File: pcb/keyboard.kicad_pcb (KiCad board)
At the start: 2 copper layers, 6 parts

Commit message: Modified layout further
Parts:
- removed H1, H2, H3, H4, H5, H6: MountingHole, MountingHole:MountingHole_3.2mm_M3
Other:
- board outline added: 242.5 x 98.2 mm

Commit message: Working on schematic and PCB
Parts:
- added C1: 1u, Capacitor_SMD:C_0402_1005Metric, F.Cu at (153.3, 238.3)
- added C10: 4.7u, Capacitor_SMD:C_0603_1608Metric, F.Cu at (149.8, 200.7)
- added C11: 100nF, Capacitor_SMD:C_0603_1608Metric, F.Cu at (149.8, 203.2)
- added C2: 100nF, Capacitor_SMD:C_0603_1608Metric, F.Cu at (153.9, 236.1)
- added C3: 1u, Capacitor_SMD:C_0402_1005Metric, F.Cu at (153.3, 240.3)
- added C4: 33p, Capacitor_SMD:C_0805_2012Metric, F.Cu at (160.7, 205.4)
- added C5: 33p, Capacitor_SMD:C_0805_2012Metric, F.Cu at (160.7, 208.4)
- added C6: 10n, Capacitor_SMD:C_0603_1608Metric, F.Cu at (149.8, 190.7)
- added C7: 100nF, Capacitor_SMD:C_0603_1608Metric, F.Cu at (149.8, 193.2)
- added C8: 100nF, Capacitor_SMD:C_0603_1608Metric, F.Cu at (149.8, 195.7)
- added C9: 1u, Capacitor_SMD:C_0603_1608Metric, F.Cu at (149.8, 198.2)
- added D1: D_Small, Diode_SMD:D_SOD-123, F.Cu at (35.7, 270.1)
- added D10: D_Small, Diode_SMD:D_SOD-123, F.Cu at (41.5, 270.1)
- added D11: D_Small, Diode_SMD:D_SOD-123, F.Cu at (41.5, 273.4)
- added D12: D_Small, Diode_SMD:D_SOD-123, F.Cu at (41.5, 276.8)
- added D13: D_Small, Diode_SMD:D_SOD-123, F.Cu at (41.5, 280.1)
- added D14: D_Small, Diode_SMD:D_SOD-123, F.Cu at (41.5, 283.5)
- added D15: D_Small, Diode_SMD:D_SOD-123, F.Cu at (41.5, 286.9)
- added D16: D_Small, Diode_SMD:D_SOD-123, F.Cu at (41.5, 290.2)
- added D17: D_Small, Diode_SMD:D_SOD-123, F.Cu at (41.5, 293.6)
- added D18: D_Small, Diode_SMD:D_SOD-123, F.Cu at (41.5, 296.9)
- added D19: D_Small, Diode_SMD:D_SOD-123, F.Cu at (47.3, 270.1)
- added D2: D_Small, Diode_SMD:D_SOD-123, F.Cu at (35.7, 273.4)
- added D20: D_Small, Diode_SMD:D_SOD-123, F.Cu at (47.3, 273.4)
- added D21: D_Small, Diode_SMD:D_SOD-123, F.Cu at (47.3, 276.8)
- added D22: D_Small, Diode_SMD:D_SOD-123, F.Cu at (47.3, 280.1)
- added D23: D_Small, Diode_SMD:D_SOD-123, F.Cu at (47.3, 283.5)
- added D24: D_Small, Diode_SMD:D_SOD-123, F.Cu at (47.3, 286.9)
- added D25: D_Small, Diode_SMD:D_SOD-123, F.Cu at (47.3, 290.2)
- added D26: D_Small, Diode_SMD:D_SOD-123, F.Cu at (47.3, 293.6)
- added D27: D_Small, Diode_SMD:D_SOD-123, F.Cu at (47.3, 296.9)
- added D28: D_Small, Diode_SMD:D_SOD-123, F.Cu at (53.1, 270.1)
- added D29: D_Small, Diode_SMD:D_SOD-123, F.Cu at (53.1, 273.4)
- added D3: D_Small, Diode_SMD:D_SOD-123, F.Cu at (35.7, 276.8)
- added D30: D_Small, Diode_SMD:D_SOD-123, F.Cu at (53.1, 276.8)
- added D31: D_Small, Diode_SMD:D_SOD-123, F.Cu at (53.1, 280.1)
- added D32: D_Small, Diode_SMD:D_SOD-123, F.Cu at (53.1, 283.5)
- added D33: D_Small, Diode_SMD:D_SOD-123, F.Cu at (53.1, 286.9)
- added D34: D_Small, Diode_SMD:D_SOD-123, F.Cu at (53.1, 290.2)
- added D35: D_Small, Diode_SMD:D_SOD-123, F.Cu at (53.1, 293.6)
- added D36: D_Small, Diode_SMD:D_SOD-123, F.Cu at (53.1, 296.9)
- added D37: D_Small, Diode_SMD:D_SOD-123, F.Cu at (58.9, 270.1)
- added D38: D_Small, Diode_SMD:D_SOD-123, F.Cu at (58.9, 273.4)
- added D39: D_Small, Diode_SMD:D_SOD-123, F.Cu at (58.9, 276.8)
- added D4: D_Small, Diode_SMD:D_SOD-123, F.Cu at (35.7, 280.1)
- added D40: D_Small, Diode_SMD:D_SOD-123, F.Cu at (58.9, 280.1)
- added D41: D_Small, Diode_SMD:D_SOD-123, F.Cu at (58.9, 283.5)
- added D42: D_Small, Diode_SMD:D_SOD-123, F.Cu at (58.9, 286.9)
- added D5: D_Small, Diode_SMD:D_SOD-123, F.Cu at (35.7, 283.5)
- added D6: D_Small, Diode_SMD:D_SOD-123, F.Cu at (35.7, 286.9)
- added D7: D_Small, Diode_SMD:D_SOD-123, F.Cu at (35.7, 290.2)
- added D8: D_Small, Diode_SMD:D_SOD-123, F.Cu at (35.7, 293.6)
- added D9: D_Small, Diode_SMD:D_SOD-123, F.Cu at (35.7, 296.9)
- added H1: MountingHole, MountingHole:MountingHole_3.2mm_M3, F.Cu at (105.0, 55.3)
- added H2: MountingHole, MountingHole:MountingHole_3.2mm_M3, F.Cu at (116.4, 113.7)
- added H3: MountingHole, MountingHole:MountingHole_3.2mm_M3, F.Cu at (200.0, 76.3)
- added H4: MountingHole, MountingHole:MountingHole_3.2mm_M3, F.Cu at (200.0, 136.1)
- added H5: MountingHole, MountingHole:MountingHole_3.2mm_M3, F.Cu at (295.0, 55.3)
- added H6: MountingHole, MountingHole:MountingHole_3.2mm_M3, F.Cu at (283.6, 113.7)
- added J1: USB_C_Receptacle_USB2.0, local-library:TYPE-C-31-M-12, F.Cu at (157.8, 218.2)
- added J2: Conn_01x04, Connector_PinHeader_2.54mm:PinHeader_1x04_P2.54mm_Vertical, F.Cu at (150.2, 214.2)
- added L1: 10u, Inductor_SMD:L_0805_2012Metric, F.Cu at (165.2, 205.2)
- added R1: 10.2k, Resistor_SMD:R_0201_0603Metric, F.Cu at (153.7, 222.2)
- added R2: 10.2k, Resistor_SMD:R_0201_0603Metric, F.Cu at (153.7, 224.0)
- added R3: 10.2k, Resistor_SMD:R_0201_0603Metric, F.Cu at (153.7, 225.7)
- added R4: 10.2k, Resistor_SMD:R_0201_0603Metric, F.Cu at (153.7, 227.5)
- added SW1: SW_Push, local-library:SW_PG1350, F.Cu at (96.3, 64.1)
- added SW10: SW_Push, local-library:SW_PG1350, F.Cu at (148.4, 68.1)
- added SW11: SW_Push, local-library:SW_PG1350, F.Cu at (144.8, 84.9)
- added SW12: SW_Push, local-library:SW_PG1350, F.Cu at (141.2, 101.8)
- added SW13: SW_Push, local-library:SW_PG1350, F.Cu at (137.6, 118.7)
- added SW14: SW_Push, local-library:SW_PG1350, F.Cu at (164.7, 74.1)
- added SW15: SW_Push, local-library:SW_PG1350, F.Cu at (161.1, 91.0)
- added SW16: SW_Push, local-library:SW_PG1350, F.Cu at (157.5, 107.8)
- added SW17: SW_Push, local-library:SW_PG1350, F.Cu at (154.0, 124.7)
- added SW18: SW_Push, local-library:SW_PG1350, F.Cu at (182.0, 75.7)
- added SW19: SW_Push, local-library:SW_PG1350, F.Cu at (178.4, 92.6)
- added SW2: SW_Push, local-library:SW_PG1350, F.Cu at (92.7, 81.0)
- added SW20: SW_Push, local-library:SW_PG1350, F.Cu at (174.8, 109.5)
- added SW21: SW_Push, local-library:SW_PG1350, F.Cu at (177.9, 133.6)
- added SW22: SW_Push, local-library:SW_PG1350, F.Cu at (218.0, 75.7)
- added SW23: SW_Push, local-library:SW_PG1350, F.Cu at (221.6, 92.6)
- added SW24: SW_Push, local-library:SW_PG1350, F.Cu at (225.2, 109.5)
- added SW25: SW_Push, local-library:SW_PG1350, F.Cu at (222.1, 133.6)
- added SW26: SW_Push, local-library:SW_PG1350, F.Cu at (235.3, 74.1)
- added SW27: SW_Push, local-library:SW_PG1350, F.Cu at (238.9, 91.0)
- added SW28: SW_Push, local-library:SW_PG1350, F.Cu at (242.5, 107.8)
- added SW29: SW_Push, local-library:SW_PG1350, F.Cu at (246.0, 124.7)
- added SW3: SW_Push, local-library:SW_PG1350, F.Cu at (89.1, 97.9)
- added SW30: SW_Push, local-library:SW_PG1350, F.Cu at (251.6, 68.1)
- added SW31: SW_Push, local-library:SW_PG1350, F.Cu at (255.2, 84.9)
- added SW32: SW_Push, local-library:SW_PG1350, F.Cu at (258.8, 101.8)
- added SW33: SW_Push, local-library:SW_PG1350, F.Cu at (262.4, 118.7)
- added SW34: SW_Push, local-library:SW_PG1350, F.Cu at (269.0, 66.9)
- added SW35: SW_Push, local-library:SW_PG1350, F.Cu at (272.6, 83.8)
- added SW36: SW_Push, local-library:SW_PG1350, F.Cu at (276.2, 100.7)
- added SW37: SW_Push, local-library:SW_PG1350, F.Cu at (286.4, 65.8)
- added SW38: SW_Push, local-library:SW_PG1350, F.Cu at (290.0, 82.6)
- added SW39: SW_Push, local-library:SW_PG1350, F.Cu at (293.6, 99.5)
- added SW4: SW_Push, local-library:SW_PG1350, F.Cu at (113.6, 65.8)
- added SW40: SW_Push, local-library:SW_PG1350, F.Cu at (303.7, 64.1)
- added SW41: SW_Push, local-library:SW_PG1350, F.Cu at (307.3, 81.0)
- added SW42: SW_Push, local-library:SW_PG1350, F.Cu at (310.9, 97.9)
- added SW5: SW_Push, local-library:SW_PG1350, F.Cu at (110.0, 82.6)
- added SW6: SW_Push, local-library:SW_PG1350, F.Cu at (106.4, 99.5)
- added SW7: SW_Push, local-library:SW_PG1350, F.Cu at (131.0, 66.9)
- added SW8: SW_Push, local-library:SW_PG1350, F.Cu at (127.4, 83.8)
- added SW9: SW_Push, local-library:SW_PG1350, F.Cu at (123.8, 100.7)
- added TP1: TestPoint, TestPoint:TestPoint_Pad_D2.0mm, F.Cu at (149.8, 232.4)
- added TP2: TestPoint, TestPoint:TestPoint_Pad_D2.0mm, F.Cu at (149.8, 236.4)
- added TP3: TestPoint, TestPoint:TestPoint_Pad_D2.0mm, F.Cu at (149.8, 240.5)
- added U1: LP3993-33B3F, Package_TO_SOT_SMD:SOT-23, F.Cu at (154.3, 232.6)
- added U2: USBLC6-2SC6, Package_TO_SOT_SMD:SOT-23-6, F.Cu at (157.5, 223.6)
- added U3: STM32F411RETx, Package_QFP:LQFP-64_10x10mm_P0.5mm, F.Cu at (159.1, 196.7)
- added Y1: 12MHz, Crystal:Crystal_SMD_5032-4Pin_5.0x3.2mm, F.Cu at (155.2, 206.3)

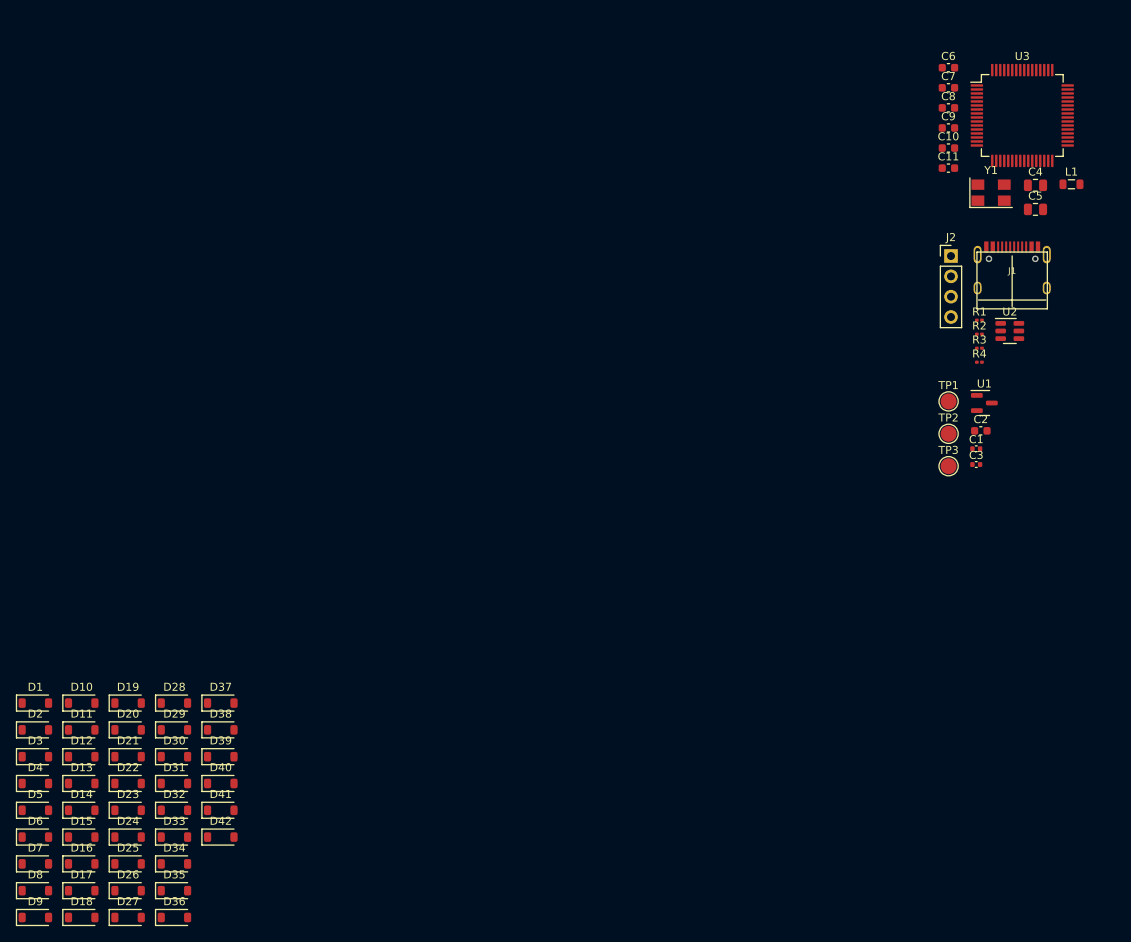
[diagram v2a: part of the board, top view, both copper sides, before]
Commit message: Finished off schematic
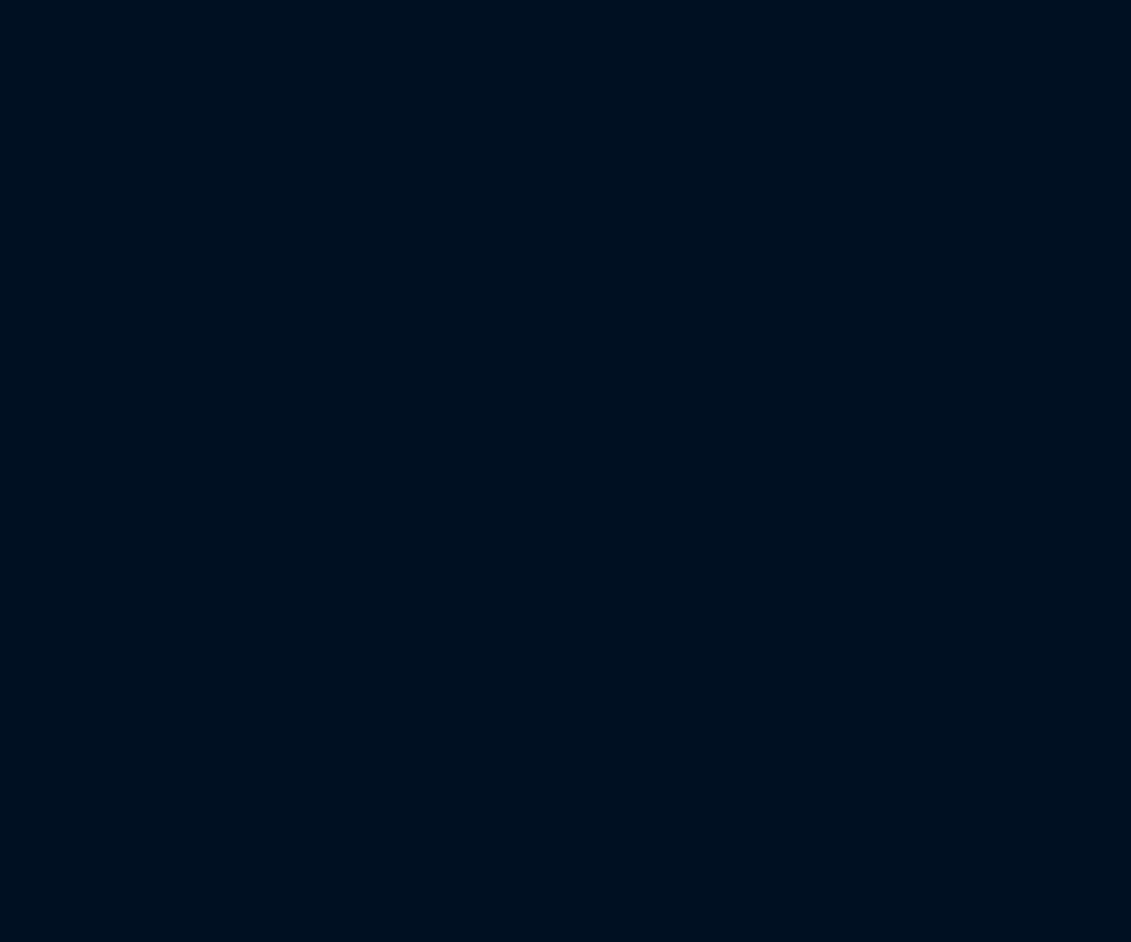
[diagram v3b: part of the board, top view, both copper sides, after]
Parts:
- removed C1, C3: 1u, Capacitor_SMD:C_0402_1005Metric
- removed C10: 4.7u, Capacitor_SMD:C_0603_1608Metric
- removed C11, C2, C7, C8: 100nF, Capacitor_SMD:C_0603_1608Metric
- removed C4, C5: 33p, Capacitor_SMD:C_0805_2012Metric
- removed C6: 10n, Capacitor_SMD:C_0603_1608Metric
- removed C9: 1u, Capacitor_SMD:C_0603_1608Metric
- removed D1, D10, D11, D12, D13, D14, D15, D16, D17, D18, D19, D2, D20, D21, D22, D23, D24, D25, D26, D27, D28, D29, D3, D30, D31, D32, D33, D34, D35, D36, D37, D38, D39, D4, D40, D41, D42, D5, D6, D7, D8, D9: D_Small, Diode_SMD:D_SOD-123
- removed J1: USB_C_Receptacle_USB2.0, local-library:TYPE-C-31-M-12
- removed J2: Conn_01x04, Connector_PinHeader_2.54mm:PinHeader_1x04_P2.54mm_Vertical
- removed L1: 10u, Inductor_SMD:L_0805_2012Metric
- removed R1, R2, R3, R4: 10.2k, Resistor_SMD:R_0201_0603Metric
- removed TP1, TP2, TP3: TestPoint, TestPoint:TestPoint_Pad_D2.0mm
- removed U1: LP3993-33B3F, Package_TO_SOT_SMD:SOT-23
- removed U2: USBLC6-2SC6, Package_TO_SOT_SMD:SOT-23-6
- removed U3: STM32F411RETx, Package_QFP:LQFP-64_10x10mm_P0.5mm
- removed Y1: 12MHz, Crystal:Crystal_SMD_5032-4Pin_5.0x3.2mm

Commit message: Started routing
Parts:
- added C1: 10n, Capacitor_SMD:C_0603_1608Metric, F.Cu at (192.5, 83.3)
- added C10: 10n, Capacitor_SMD:C_0603_1608Metric, F.Cu at (191.1, 97.6)
- added C11: 100nF, Capacitor_SMD:C_0603_1608Metric, F.Cu at (191.1, 102.4)
- added C12: 100nF, Capacitor_SMD:C_0603_1608Metric, F.Cu at (203.9, 107.7)
- added C13: 1u, Capacitor_SMD:C_0603_1608Metric, F.Cu at (211.8, 97.2)
- added C14: 4.7u, Capacitor_SMD:C_0603_1608Metric, F.Cu at (208.3, 102.8)
- added C15: 100nF, Capacitor_SMD:C_0603_1608Metric, B.Cu at (199.7, 102.0)
- added C16: 1u, Capacitor_SMD:C_0603_1608Metric, F.Cu at (197.5, 89.0)
- added C2: 100n, Capacitor_SMD:C_0603_1608Metric, F.Cu at (196.5, 83.3)
- added C3: 10u, Capacitor_SMD:C_0805_2012Metric, F.Cu at (194.5, 86.2)
- added C4: 1u, Capacitor_SMD:C_0603_1608Metric, F.Cu at (191.5, 86.8)
- added C5: 100nF, Capacitor_SMD:C_0603_1608Metric, F.Cu at (191.5, 90.2)
- added C6: 33p, Capacitor_SMD:C_0805_2012Metric, F.Cu at (195.8, 111.8)
- added C7: 15p, Capacitor_SMD:C_0805_2012Metric, F.Cu at (196.5, 115.8)
- added C8: 33p, Capacitor_SMD:C_0805_2012Metric, F.Cu at (204.2, 111.8)
- added C9: 15p, Capacitor_SMD:C_0805_2012Metric, F.Cu at (203.5, 115.8)
- added D1: D_Small, Diode_SMD:D_SOD-123, B.Cu at (101.4, 70.5)
- added D10: D_Small, Diode_SMD:D_SOD-123, B.Cu at (153.5, 74.4)
- added D11: D_Small, Diode_SMD:D_SOD-123, B.Cu at (149.9, 91.3)
- added D12: D_Small, Diode_SMD:D_SOD-123, B.Cu at (146.3, 108.2)
- added D13: D_Small, Diode_SMD:D_SOD-123, B.Cu at (142.7, 125.0)
- added D14: D_Small, Diode_SMD:D_SOD-123, B.Cu at (169.9, 80.4)
- added D15: D_Small, Diode_SMD:D_SOD-123, B.Cu at (166.3, 97.3)
- added D16: D_Small, Diode_SMD:D_SOD-123, B.Cu at (162.7, 114.2)
- added D17: D_Small, Diode_SMD:D_SOD-123, B.Cu at (159.1, 131.1)
- added D18: D_Small, Diode_SMD:D_SOD-123, B.Cu at (187.1, 82.1)
- added D19: D_Small, Diode_SMD:D_SOD-123, B.Cu at (183.6, 98.9)
- added D2: D_Small, Diode_SMD:D_SOD-123, B.Cu at (97.8, 87.4)
- added D20: D_Small, Diode_SMD:D_SOD-123, B.Cu at (180.0, 115.8)
- added D21: D_Small, Diode_SMD:D_SOD-123, B.Cu at (181.2, 141.1)
- added D22: D_Small, Diode_SMD:D_SOD-123, B.Cu at (225.3, 79.4)
- added D23: D_Small, Diode_SMD:D_SOD-123, B.Cu at (228.9, 96.3)
- added D24: D_Small, Diode_SMD:D_SOD-123, B.Cu at (232.5, 113.2)
- added D25: D_Small, Diode_SMD:D_SOD-123, B.Cu at (230.1, 135.3)
- added D26: D_Small, Diode_SMD:D_SOD-123, B.Cu at (242.6, 77.8)
- added D27: D_Small, Diode_SMD:D_SOD-123, B.Cu at (246.2, 94.7)
- added D28: D_Small, Diode_SMD:D_SOD-123, B.Cu at (249.7, 111.5)
- added D29: D_Small, Diode_SMD:D_SOD-123, B.Cu at (253.3, 128.4)
- added D3: D_Small, Diode_SMD:D_SOD-123, B.Cu at (94.3, 104.2)
- added D30: D_Small, Diode_SMD:D_SOD-123, B.Cu at (258.9, 71.8)
- added D31: D_Small, Diode_SMD:D_SOD-123, B.Cu at (262.5, 88.6)
- added D32: D_Small, Diode_SMD:D_SOD-123, B.Cu at (266.1, 105.5)
- added D33: D_Small, Diode_SMD:D_SOD-123, B.Cu at (269.7, 122.4)
- added D34: D_Small, Diode_SMD:D_SOD-123, B.Cu at (276.3, 70.6)
- added D35: D_Small, Diode_SMD:D_SOD-123, B.Cu at (279.9, 87.5)
- added D36: D_Small, Diode_SMD:D_SOD-123, B.Cu at (283.5, 104.4)
- added D37: D_Small, Diode_SMD:D_SOD-123, B.Cu at (293.7, 69.5)
- added D38: D_Small, Diode_SMD:D_SOD-123, B.Cu at (297.3, 86.4)
- added D39: D_Small, Diode_SMD:D_SOD-123, B.Cu at (300.9, 103.2)
- added D4: D_Small, Diode_SMD:D_SOD-123, B.Cu at (118.7, 72.1)
- added D40: D_Small, Diode_SMD:D_SOD-123, B.Cu at (311.0, 67.9)
- added D41: D_Small, Diode_SMD:D_SOD-123, B.Cu at (314.6, 84.7)
- added D42: D_Small, Diode_SMD:D_SOD-123, B.Cu at (318.2, 101.6)
- added D5: D_Small, Diode_SMD:D_SOD-123, B.Cu at (115.1, 89.0)
- added D6: D_Small, Diode_SMD:D_SOD-123, B.Cu at (111.5, 105.9)
- added D7: D_Small, Diode_SMD:D_SOD-123, B.Cu at (136.1, 73.3)
- added D8: D_Small, Diode_SMD:D_SOD-123, B.Cu at (132.5, 90.1)
- added D9: D_Small, Diode_SMD:D_SOD-123, B.Cu at (128.9, 107.0)
- added FB1: FerriteBead_Small, Inductor_SMD:L_0603_1608Metric, F.Cu at (194.5, 83.0)
- added J1: USB_C_Receptacle_USB2.0, local-library:TYPE-C-31-M-12, F.Cu at (200.0, 62.5)
- added J2: Conn_01x04, Connector_PinSocket_2.54mm:PinSocket_1x04_P2.54mm_Vertical, B.Cu at (191.8, 47.8)
- added JP1: bridge, Jumper:SolderJumper-2_P1.3mm_Open_RoundedPad1.0x1.5mm, B.Cu at (89.2, 69.0)
- added JP2: bridge, Jumper:SolderJumper-2_P1.3mm_Open_RoundedPad1.0x1.5mm, B.Cu at (77.8, 67.2)
- added L1: 10u, Inductor_SMD:L_0805_2012Metric, B.Cu at (200.0, 103.8)
- added Q2: BC858, Package_TO_SOT_SMD:SOT-23, B.Cu at (80.8, 63.2)
- added R1: 10.2k, Resistor_SMD:R_0603_1608Metric, F.Cu at (204.2, 70.5)
- added R2: 10.2k, Resistor_SMD:R_0603_1608Metric, F.Cu at (206.2, 70.5)
- added R3: 10.2k, Resistor_SMD:R_0603_1608Metric, F.Cu at (195.8, 70.5)
- added R4: 10.2k, Resistor_SMD:R_0603_1608Metric, F.Cu at (193.8, 70.5)
- added R5: 10.2k, Resistor_SMD:R_0201_0603Metric, B.Cu at (81.3, 53.4)
- added R7: 1.91k, Resistor_SMD:R_0201_0603Metric, B.Cu at (84.8, 62.5)
- added R8: 10.2k, Resistor_SMD:R_0201_0603Metric, B.Cu at (80.6, 56.9)
- added TP1: ~, TestPoint:TestPoint_Pad_D2.0mm, F.Cu at (190.5, 66.8)
- added TP2: ~, TestPoint:TestPoint_Pad_D2.0mm, F.Cu at (194.2, 78.2)
- added TP3: ~, TestPoint:TestPoint_Pad_D2.0mm, F.Cu at (200.0, 143.3)
- added TP4: ~, TestPoint:TestPoint_Pad_D2.0mm, F.Cu at (188.9, 100.0)
- added U1: LP3993-33B3F, Package_TO_SOT_SMD:SOT-23, F.Cu at (194.5, 89.5)
- added U2: USBLC6-2SC6, Package_TO_SOT_SMD:SOT-23-6, F.Cu at (200.0, 71.0)
- added U3: STM32F411RETx, Package_QFP:LQFP-64_10x10mm_P0.5mm, F.Cu at (200.0, 100.0)
- added Y1: 12MHz, Crystal:Crystal_SMD_5032-4Pin_5.0x3.2mm, F.Cu at (200.0, 111.8)
- added Y2: 32.768k, Crystal:Crystal_SMD_3215-2Pin_3.2x1.5mm, F.Cu at (200.0, 115.8)
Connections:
- net col1 renamed /inputs/col1
- net col10 renamed /inputs/col10
- net col11 renamed /inputs/col11
- net col2 renamed /inputs/col2
- net col3 renamed /inputs/col3
- net col4 renamed /inputs/col4
- net col5 renamed /inputs/col5
- net col6 renamed /inputs/col6
- net col7 renamed /inputs/col7
- net col8 renamed /inputs/col8
- net col9 renamed /inputs/col9
- SW1 pad 2: col0 -> Net-(JP1-A)
- SW2 pad 2: col0 -> /inputs/col0
- SW3 pad 2: col0 -> /inputs/col0
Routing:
- net VBUS: track 0.00 -> 49.9 mm, vias 0 -> 2
- net +3V3: track 0.00 -> 46.5 mm, vias 0 -> 1
- net /connectors/USB_D+: track 0.00 -> 31.8 mm, vias 0 -> 2
- net /connectors/USB_D-: track 0.00 -> 27.6 mm, vias 0 -> 2
- net /stm32/LSEO_OUT: track 0.00 -> 21.8 mm
- net /stm32/LSEO_IN: track 0.00 -> 17.6 mm
- net /stm32/HSEO_OUT: track 0.00 -> 14.1 mm
- net /stm32/HSEO_IN: track 0.00 -> 13.5 mm
- net /connectors/CC1: track 0.00 -> 6.45 mm
- net +5V: track 0.00 -> 6.13 mm
- net /connectors/CC2: track 0.00 -> 5.93 mm
- net Net-(J1-D--PadA7): track 0.00 -> 5.39 mm
- net Net-(J1-D+-PadA6): track 0.00 -> 5.39 mm
- net Net-(U3-VDDA): track 0.00 -> 4.50 mm, vias 0 -> 1
- net GND: track 0.00 -> 4.06 mm, vias 0 -> 1
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- added copper zone on F.Cu, net +5V
- added copper zone on F.Cu, net GND
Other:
- outline, holes or cut-outs redrawn
- board text added: "3.3V"
- board text added: "5V"
- board text added: "GND"
- board text added: "JLCJLCJLCJLC"
- board text added: "VBUS"

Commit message: Continued routing
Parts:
- moved TP1 58.6 mm to (194.3, 125.2)
- moved TP2 47.2 mm to (198.1, 125.2)
- moved TP4 28.4 mm to (201.8, 125.2)
- moved TP3 18.9 mm to (205.6, 125.2)
- moved C13 13.4 mm to (200.0, 90.8), turned to 180 degrees
- moved C1 5.77 mm to (198.0, 81.6)
- moved C2 5.77 mm to (202.0, 81.6)
- moved C3 5.77 mm to (200.0, 84.5)
- moved C4 5.77 mm to (197.0, 85.0)
- moved C5 5.77 mm to (197.0, 88.5)
- moved FB1 5.77 mm to (200.0, 81.2)
- moved U1 5.77 mm to (200.0, 87.8)
- moved C16 5.52 mm to (203.0, 88.5)
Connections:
- C16 pad 1: +3.3V -> +3V3
- JP1 pad 2: +3.3V -> +3V3
- TP4 pad 1: +3.3V -> +3V3
- U1 pad 2: +3.3V -> +3V3
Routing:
- net /inputs/row0: track 0.00 -> 266.6 mm, vias 0 -> 1
- net /inputs/row2: track 0.00 -> 255.4 mm, vias 0 -> 1
- net /inputs/row1: track 0.00 -> 236.5 mm, vias 0 -> 1
- net /inputs/row3: track 0.00 -> 183.6 mm, vias 0 -> 1
- net /inputs/col6: track 0.00 -> 62.5 mm
- net /inputs/col5: track 0.00 -> 60.4 mm
- net /inputs/col7: track 0.00 -> 56.0 mm
- net /inputs/col4: track 0.00 -> 55.4 mm
- net /inputs/col8: track 0.00 -> 55.1 mm
- net /inputs/col3: track 0.00 -> 55.1 mm
- net +5V: track 6.13 -> 47.2 mm
- net /inputs/col1: track 0.00 -> 37.5 mm
- net /inputs/col11: track 0.00 -> 36.7 mm
- net /inputs/col9: track 0.00 -> 36.7 mm
- net /inputs/col2: track 0.00 -> 36.7 mm
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
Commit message: Finished routing, ready for checks
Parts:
- added C17: 0.1u, Capacitor_SMD:C_0603_1608Metric, F.Cu at (194.5, 121.5)
- added SW43: TS-1187A-B-A-B, Button_Switch_SMD:SW_Push_1P1T_NO_CK_KSC6xxJ, F.Cu at (200.0, 121.8)
- J2: footprint Connector_PinSocket_2.54mm:PinSocket_1x04_P2.54mm_Vertical -> Connector_PinSocket_2.54mm:PinSocket_1x04_P2.54mm_Horizontal
- R5, R7, R8: footprint Resistor_SMD:R_0201_0603Metric -> Resistor_SMD:R_0603_1608Metric
- moved J2 91.8 mm to (203.8, 138.8), turned to 90 degrees
- moved R5 25.2 mm to (94.8, 74.8)
- moved R8 24.1 mm to (98.5, 73.0), turned to -102 degrees
- moved Q2 18.7 mm to (98.5, 69.2)
- moved JP2 14.8 mm to (92.2, 70.2)
- moved R7 14.5 mm to (95.2, 72.5)
- moved H4 3.00 mm to (200.0, 133.1)
- moved TP1 2.00 mm to (194.3, 127.2)
- moved TP2 2.00 mm to (198.1, 127.2)
- moved TP3 2.00 mm to (205.6, 127.2)
- moved TP4 2.00 mm to (201.8, 127.2)
- moved JP1 0.90 mm to (88.5, 69.5)
- moved C14 0.28 mm to (208.5, 103.0)
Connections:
- U3 pad 7: unconnected-(U3-NRST-Pad7) -> /inputs/NRST
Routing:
- net /inputs/col0: track 18.4 -> 179.0 mm, vias 0 -> 4
- net /inputs/col11: track 36.7 -> 175.5 mm
- net /inputs/col1: track 37.5 -> 162.0 mm, vias 0 -> 2
- net +3V3: track 70.2 -> 194.3 mm, vias 1 -> 2
- net /inputs/col10: track 36.7 -> 154.1 mm
- net /inputs/BOOT0: track 0.00 -> 116.7 mm, vias 0 -> 1
- net /inputs/col2: track 36.7 -> 139.6 mm, vias 0 -> 2
- net /inputs/col9: track 36.7 -> 134.5 mm
- net /inputs/col3: track 55.1 -> 138.5 mm, vias 0 -> 2
- net /inputs/col8: track 55.1 -> 127.5 mm
- net /inputs/col4: track 55.4 -> 122.9 mm, vias 0 -> 2
- net /connectors/SWCLK: track 0.00 -> 53.1 mm, vias 0 -> 5
- net /connectors/SWDIO: track 0.00 -> 49.8 mm, vias 0 -> 3
- net /inputs/col7: track 56.0 -> 96.7 mm
- net /inputs/col5: track 60.4 -> 97.6 mm, vias 0 -> 2
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- added copper zone on F.Cu, net +3V3
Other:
- board text added: "SWCLK"
- board text added: "SWDIO"

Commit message: Creating production files
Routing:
- net +3V3: track 194.3 -> 195.0 mm
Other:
- rule pad_to_mask_clearance: 0.05 -> 0
- board text added: "CLK"
- board text added: "IO"
- board text removed: "SWCLK"
- board text removed: "SWDIO"

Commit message: Added name to silkscreen, updated prod files
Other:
- board text added: "Designed by Jack Bradley"
- board text added: "Thingamaboard"
- board text added: "v1.0"
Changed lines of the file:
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@@
   (gr_arc locked (start 204.750002 61.336118) (mid 205.103566 61.48256) (end 205.250002 61.836118)
     (stroke (width 0.2) (type solid)) (layer "Edge.Cuts"))
+  (gr_text "Designed by Jack Bradley" (at 197.528558 128) (layer "B.SilkS")
+    (effects (font (size 1 1) (thickness 0.2) bold) (justify left bottom mirror))
+  )
+  (gr_text "v1.0" (at 221.528558 128.45) (layer "B.SilkS")
+    (effects (font (size 1.5 1.5) (thickness 0.375) bold) (justify left bottom mirror))
+  )
+  (gr_text "Thingamaboard" (at 222.528558 126) (layer "B.SilkS")
+    (effects (font (size 4 4) (thickness 0.8) bold italic) (justify left bottom mirror))
+  )
   (gr_text "3.3V" (at 204.3 137.45 90) (layer "F.SilkS")
     (effects (font (size 0.7 0.7) (thickness 0.175) bold) (justify left bottom))
@@
     )
   )
+  (group "" (id dd16fcc7-7701-4732-8536-5fad40a12372)
+    (members
+      3a60825b-b14f-46cc-b9f5-bb9389149328
+      8a7374ad-8f4e-469e-ae67-80aed4dcecef
+      8e67cc89-c36a-49e1-8921-6adfe749eab5
+    )
+  )
